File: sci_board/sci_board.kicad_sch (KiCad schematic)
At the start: 5 parts

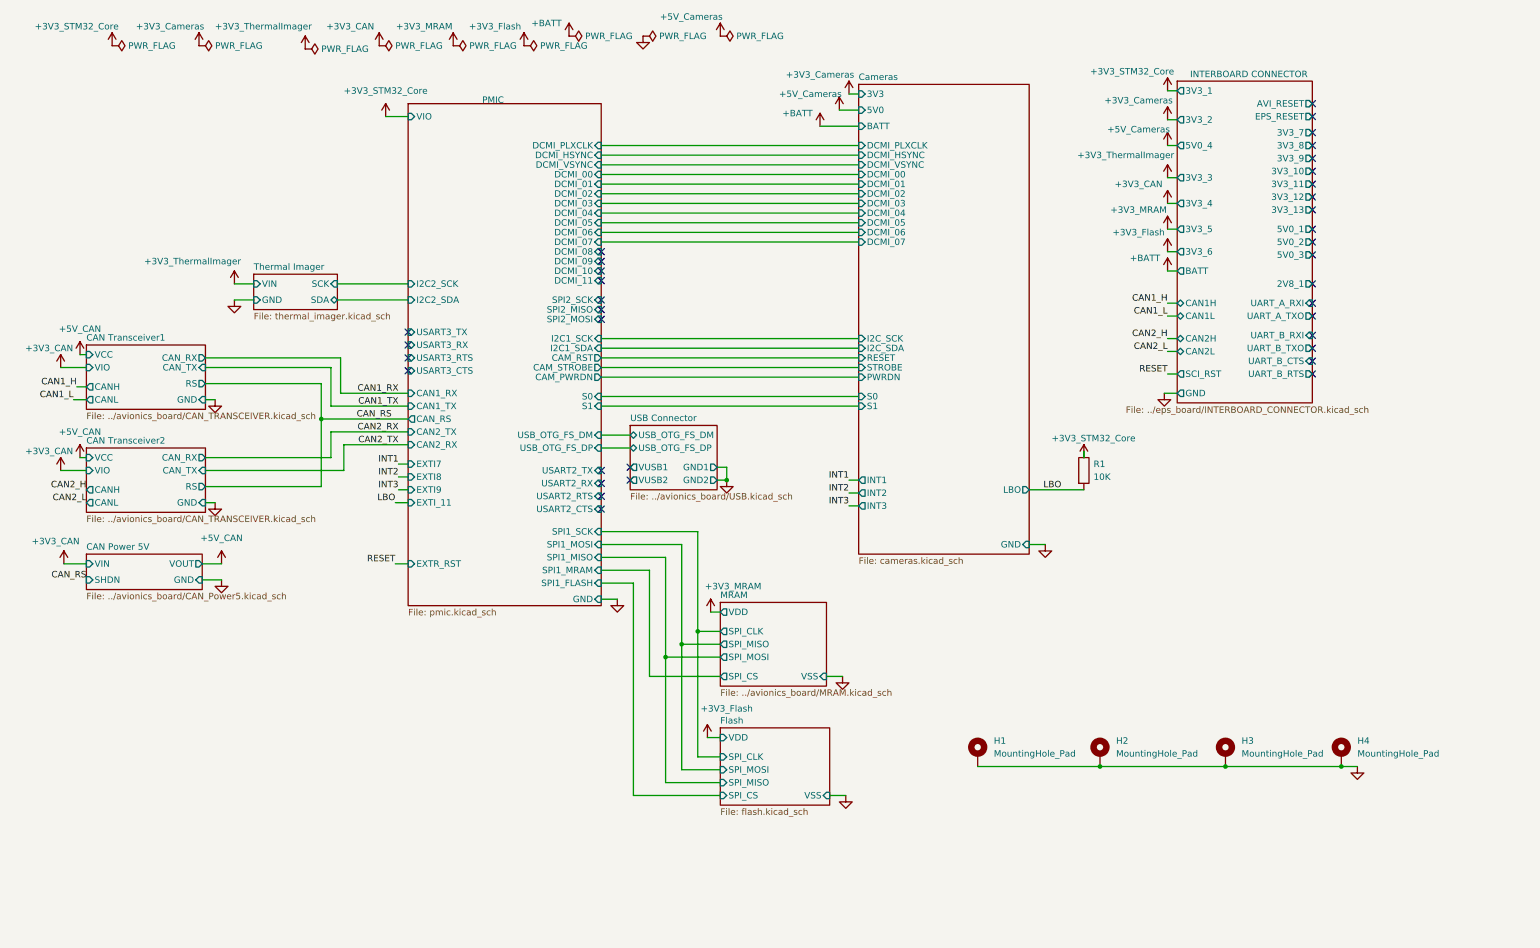
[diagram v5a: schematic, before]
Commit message: replace big multiplexers with tiny ones, replace boost converters with true ones
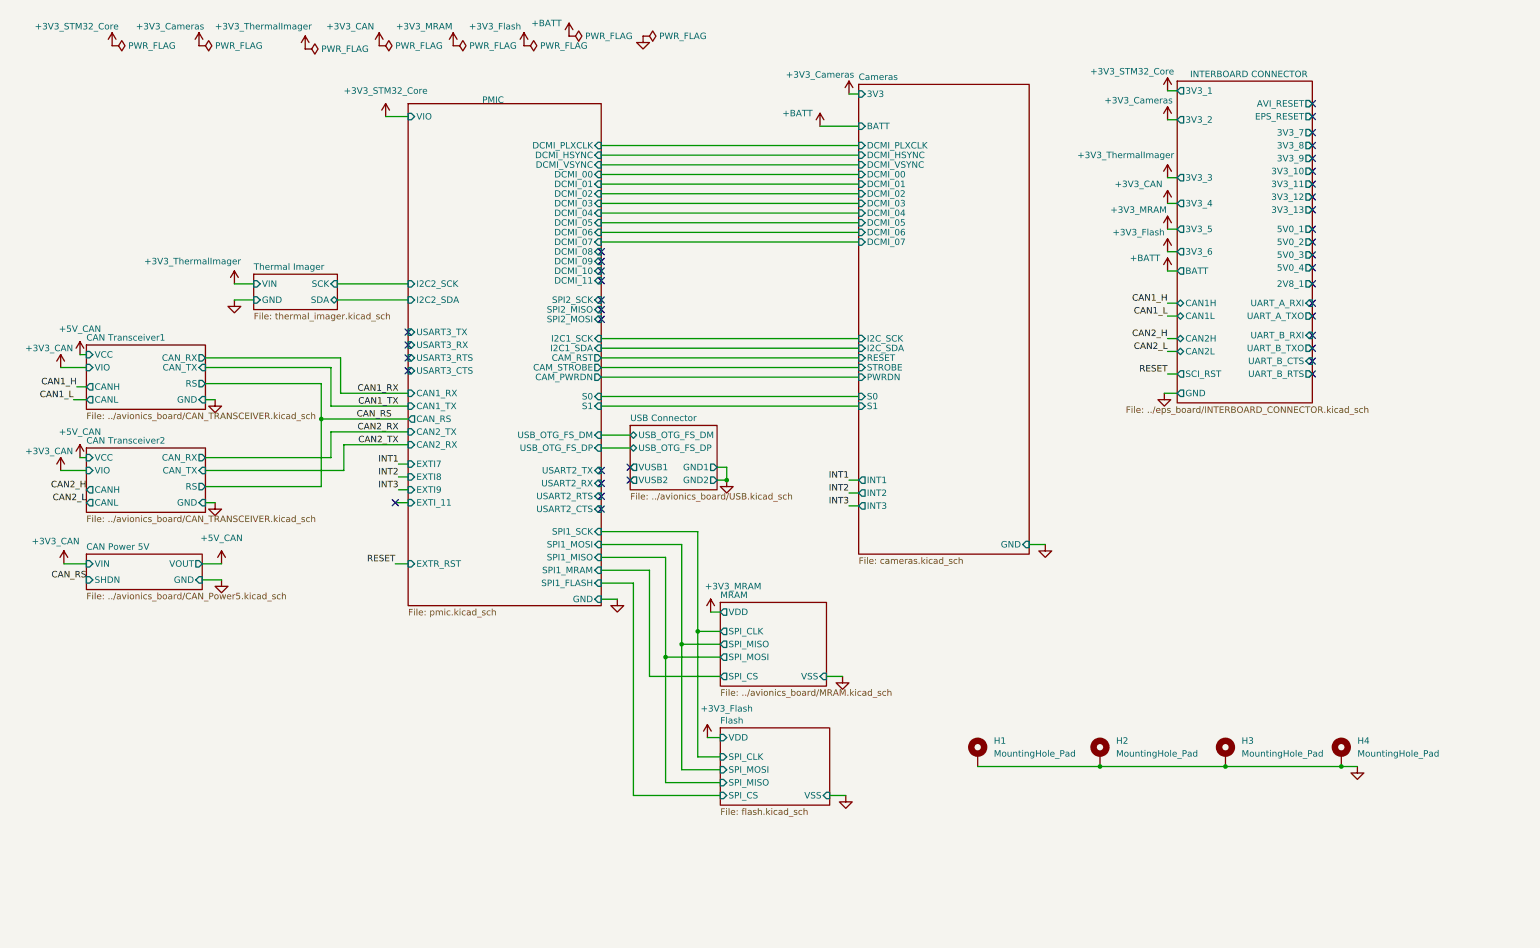
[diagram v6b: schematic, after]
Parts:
- removed R1: 10K, Resistor_SMD:R_0603_1608Metric_Pad0.98x0.95mm_HandSolder, symbol Device:R
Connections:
- no-connect marks 36 -> 38
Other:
- sheet Cameras ports: added none; removed 5V0, LBO

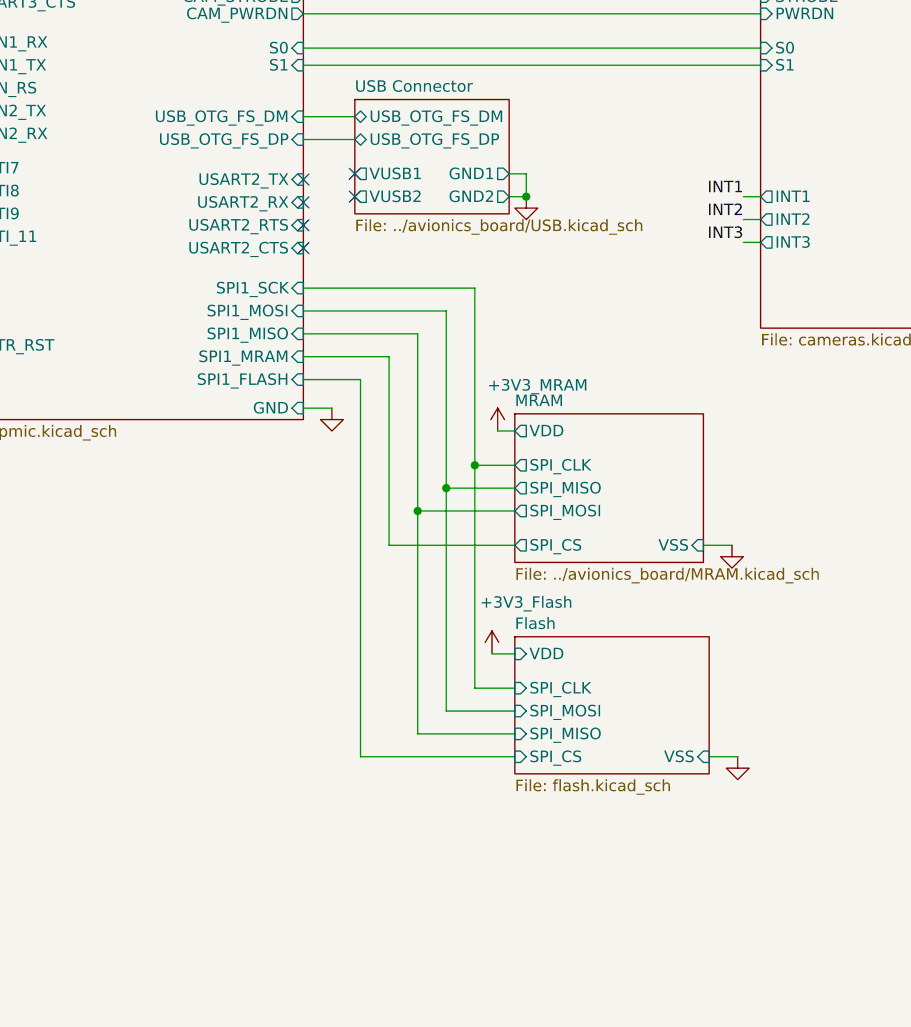
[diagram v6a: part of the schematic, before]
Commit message: changed over SCI to smaller footprint switches
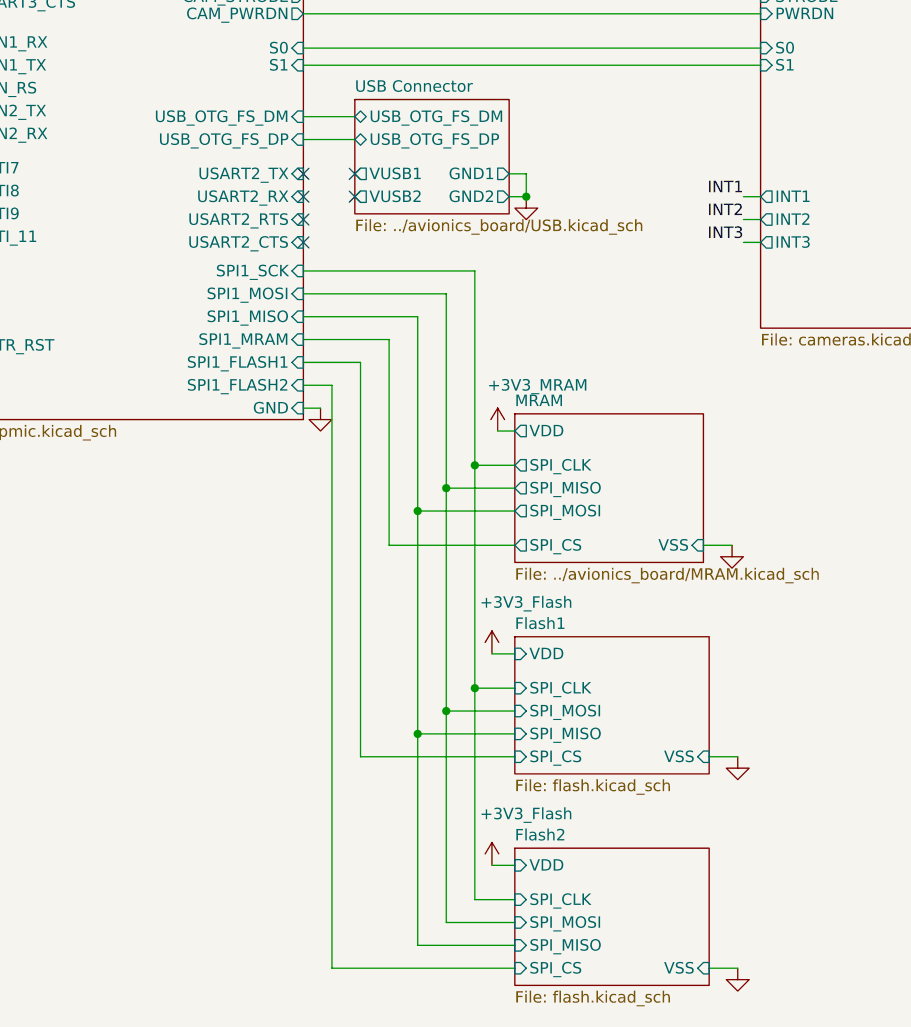
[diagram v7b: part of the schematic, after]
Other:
- sheet Flash renamed Flash1
- added sheet Flash2 (flash.kicad_sch)
- sheet PMIC ports: added SPI1_FLASH1, SPI1_FLASH2; removed SPI1_FLASH

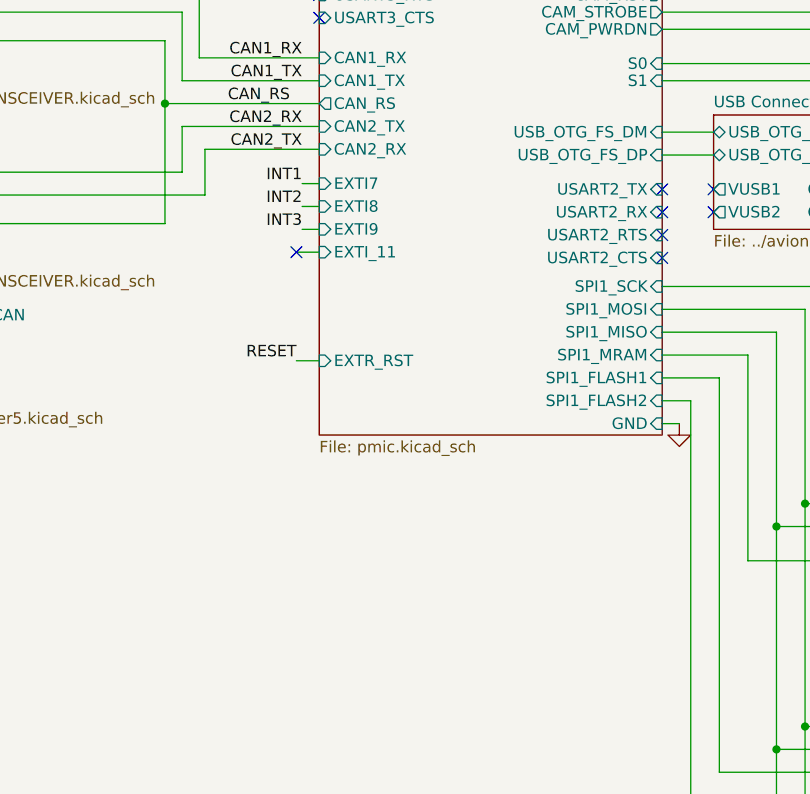
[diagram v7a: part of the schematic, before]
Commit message: replace nearly all buck converters with boost buck (missing is 5raw
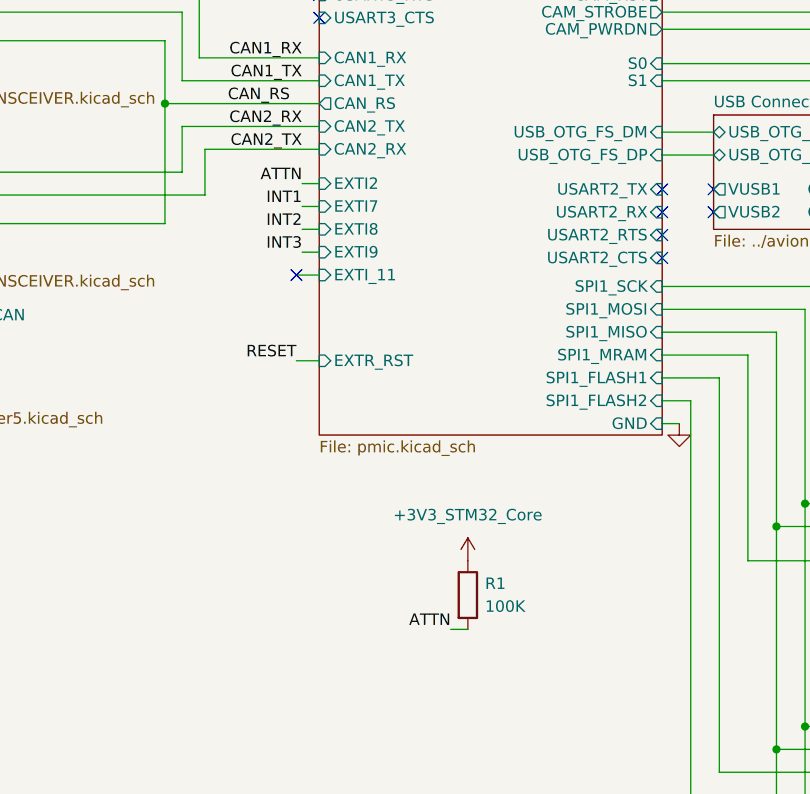
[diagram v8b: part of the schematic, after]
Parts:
- added R1: 100K, Resistor_SMD:R_0402_1005Metric_Pad0.72x0.64mm_HandSolder, symbol Device:R
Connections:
- net +3V3_STM32_Core: now also R1.1
- new net ATTN: R1.2
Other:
- sheet PMIC ports: added EXTI2; removed none
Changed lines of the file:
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@@
 	)
 	(no_connect
-		(at 85.725 110.49)
+		(at 85.725 113.03)
 	)
 	(no_connect
@@
 	(wire
 		(pts
-			(xy 86.36 105.41) (xy 88.265 105.41)
+			(xy 86.36 107.95) (xy 88.265 107.95)
 		)
 		(stroke
@@
 	(wire
 		(pts
+			(xy 86.36 102.87) (xy 88.265 102.87)
+		)
+		(stroke
+			(width 0)
+			(type default)
+		)
+	)
+	(wire
+		(pts
 			(xy 145.415 184.15) (xy 149.86 184.15)
 		)
@@
 	(wire
 		(pts
-			(xy 86.36 107.95) (xy 88.265 107.95)
+			(xy 86.36 110.49) (xy 88.265 110.49)
 		)
 		(stroke
@@
 	(wire
 		(pts
-			(xy 85.725 110.49) (xy 88.265 110.49)
+			(xy 85.725 113.03) (xy 88.265 113.03)
 		)
 		(stroke
@@
 	(wire
 		(pts
+			(xy 102.87 152.4) (xy 104.775 152.4)
+		)
+		(stroke
+			(width 0)
+			(type default)
+		)
+	)
+	(wire
+		(pts
 			(xy 19.685 83.82) (xy 24.765 83.82)
 		)
@@
 	(wire
 		(pts
-			(xy 86.36 102.87) (xy 88.265 102.87)
+			(xy 86.36 105.41) (xy 88.265 105.41)
 		)
 		(stroke
@@
 	)
 	(label "INT3"
-		(at 86.36 107.95 180)
+		(at 86.36 110.49 180)
 		(fields_autoplaced yes)
 		(effects
@@
 	)
 	(label "INT2"
-		(at 86.36 105.41 180)
+		(at 86.36 107.95 180)
 		(fields_autoplaced yes)
 		(effects
@@
 	)
 	(label "INT1"
-		(at 86.36 102.87 180)
+		(at 86.36 105.41 180)
 		(fields_autoplaced yes)
 		(effects
@@
 		)
 	)
+	(label "ATTN"
+		(at 86.36 102.87 180)
+		(fields_autoplaced yes)
+		(effects
+			(font
+				(size 1.27 1.27)
+			)
+			(justify right bottom)
+		)
+	)
 	(label "CAN2_TX"
 		(at 86.36 99.06 180)
@@
 		)
 	)
+	(label "ATTN"
+		(at 102.87 152.4 180)
+		(fields_autoplaced yes)
+		(effects
+			(font
+				(size 1.27 1.27)
+			)
+			(justify right bottom)
+		)
+	)
 	(label "CAN1_TX"
 		(at 86.36 91.44 180)
@@
 		(dnp no)
 		(fields_autoplaced yes)
-		(property "Reference" "#PWR040"
+		(property "Reference" "#PWR041"
 			(at 174.625 198.12 0)
 			(effects
@@
 			(project "sci_board"
 				(path "/b4b2c88d-f6cd-4e60-862d-e21f68728580"
-					(reference "#PWR040")
+					(reference "#PWR041")
 					(unit 1)
 				)
@@
 		(dnp no)
 		(fields_autoplaced yes)
-		(property "Reference" "#PWR035"
+		(property "Reference" "#PWR036"
 			(at 173.99 151.13 0)
 			(effects
@@
 			(project "sci_board"
 				(path "/b4b2c88d-f6cd-4e60-862d-e21f68728580"
-					(reference "#PWR035")
+					(reference "#PWR036")
 					(unit 1)
 				)
@@
 		(dnp no)
 		(fields_autoplaced yes)
-		(property "Reference" "#PWR037"
+		(property "Reference" "#PWR038"
 			(at 275.59 168.91 0)
 			(effects
@@
 			(project "sci_board"
 				(path "/b4b2c88d-f6cd-4e60-862d-e21f68728580"
-					(reference "#PWR037")
+					(reference "#PWR038")
 					(unit 1)
 				)
@@
 		(dnp no)
 		(fields_autoplaced yes)
-		(property "Reference" "#PWR038"
+		(property "Reference" "#PWR039"
 			(at 174.625 174.625 0)
 			(effects
@@
 			(project "sci_board"
 				(path "/b4b2c88d-f6cd-4e60-862d-e21f68728580"
-					(reference "#PWR038")
+					(reference "#PWR039")
 					(unit 1)
 				)
@@
 		(on_board yes)
 		(dnp no)
-		(property "Reference" "#PWR039"
+		(property "Reference" "#PWR040"
 			(at 147.32 184.15 0)
 			(effects
@@
 			(project "sci_board"
 				(path "/b4b2c88d-f6cd-4e60-862d-e21f68728580"
-					(reference "#PWR039")
+					(reference "#PWR040")
 					(unit 1)
 				)
@@
 	)
 	(symbol
+		(lib_id "Device:R")
+		(at 104.775 148.59 0)
+		(unit 1)
+		(exclude_from_sim no)
+		(in_bom yes)
+		(on_board yes)
+		(dnp no)
+		(fields_autoplaced yes)
+		(property "Reference" "R1"
+			(at 106.68 147.3199 0)
+			(effects
+				(font
+					(size 1.27 1.27)
+				)
+				(justify left)
+			)
+		)
+		(property "Value" "100K"
+			(at 106.68 149.8599 0)
+			(effects
+				(font
+					(size 1.27 1.27)
+				)
+				(justify left)
+			)
+		)
+		(property "Footprint" "Resistor_SMD:R_0402_1005Metric_Pad0.72x0.64mm_HandSolder"
+			(at 102.997 148.59 90)
+			(effects
+				(font
+					(size 1.27 1.27)
+				)
+				(hide yes)
+			)
+		)
+		(property "Datasheet" "~"
+			(at 104.775 148.59 0)
+			(effects
+				(font
+					(size 1.27 1.27)
+				)
+				(hide yes)
+			)
+		)
+		(property "Description" "Resistor"
+			(at 104.775 148.59 0)
+			(effects
+				(font
+					(size 1.27 1.27)
+				)
+				(hide yes)
+			)
+		)
+		(pin "2"
+		)
+		(pin "1"
+		)
+		(instances
+			(project ""
+				(path "/b4b2c88d-f6cd-4e60-862d-e21f68728580"
+					(reference "R1")
+					(unit 1)
+				)
+			)
+		)
+	)
+	(symbol
 		(lib_id "power:+3V3")
 		(at 147.32 156.845 0)
@@
 		(on_board yes)
 		(dnp no)
-		(property "Reference" "#PWR036"
+		(property "Reference" "#PWR037"
 			(at 147.32 160.655 0)
 			(effects
@@
 			(project "sci_board"
 				(path "/b4b2c88d-f6cd-4e60-862d-e21f68728580"
-					(reference "#PWR036")
+					(reference "#PWR037")
+					(unit 1)
+				)
+			)
+		)
+	)
+	(symbol
+		(lib_id "power:+3V3")
+		(at 104.775 144.78 0)
+		(unit 1)
+		(exclude_from_sim no)
+		(in_bom yes)
+		(on_board yes)
+		(dnp no)
+		(fields_autoplaced yes)
+		(property "Reference" "#PWR035"
+			(at 104.775 148.59 0)
+			(effects
+				(font
+					(size 1.27 1.27)
+				)
+				(hide yes)
+			)
+		)
+		(property "Value" "+3V3_STM32_Core"
+			(at 104.775 139.7 0)
+			(effects
+				(font
+					(size 1.27 1.27)
+				)
+			)
+		)
+		(property "Footprint" ""
+			(at 104.775 144.78 0)
+			(effects
+				(font
+					(size 1.27 1.27)
+				)
+				(hide yes)
+			)
+		)
+		(property "Datasheet" ""
+			(at 104.775 144.78 0)
+			(effects
+				(font
+					(size 1.27 1.27)
+				)
+				(hide yes)
+			)
+		)
+		(property "Description" "Power symbol creates a global label with name \"+3V3\""
+			(at 104.775 144.78 0)
+			(effects
+				(font
+					(size 1.27 1.27)
+				)
+				(hide yes)
+			)
+		)
+		(pin "1"
+		)
+		(instances
+			(project "sci_board"
+				(path "/b4b2c88d-f6cd-4e60-862d-e21f68728580"
+					(reference "#PWR035")
 					(unit 1)
 				)
@@
 		)
 		(pin "EXTI8" input
-			(at 88.265 105.41 180)
+			(at 88.265 107.95 180)
 			(effects
 				(font
@@
 		)
 		(pin "EXTI7" input
-			(at 88.265 102.87 180)
+			(at 88.265 105.41 180)
 			(effects
 				(font
@@
 		)
 		(pin "EXTI9" input
-			(at 88.265 107.95 180)
+			(at 88.265 110.49 180)
 			(effects
 				(font
@@
 		)
 		(pin "EXTI_11" input
-			(at 88.265 110.49 180)
+			(at 88.265 113.03 180)
 			(effects
 				(font
@@
 			)
 		)
+		(pin "EXTI2" input
+			(at 88.265 102.87 180)
+			(effects
+				(font
+					(size 1.27 1.27)
+				)
+				(justify left)
+			)
+		)
